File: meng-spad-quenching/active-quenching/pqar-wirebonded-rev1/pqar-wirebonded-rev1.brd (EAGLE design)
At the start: 46 x 46 mm, 62 parts, among them IC1 NL17SZ125, IC2 LTC1711, IC20 NC7WZ16P6X, IC3 NC7SV74K8X, IC4 BCV62, IC5 74AHC1G14DCK, IC6 SPAD, IC7 74AUC1G32DCK, IC8 74LVC1G02DCK, U1 SN74LVC1G123DCUT, X1 V_A, X2 OUT, X3 V_LOGIC, X4 I_HOLDOFF, X5 FORCE_QUENCH

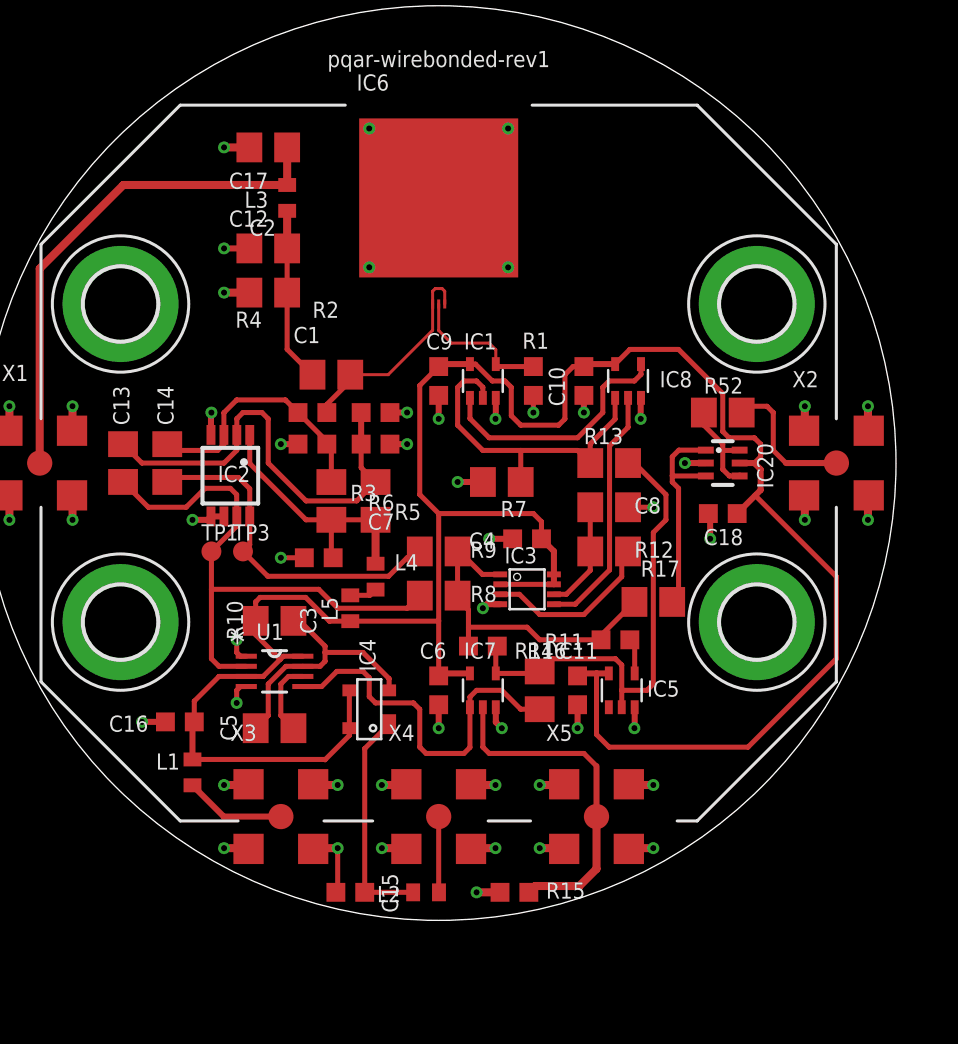
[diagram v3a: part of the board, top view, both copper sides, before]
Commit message: Clean up routing, DRC pass
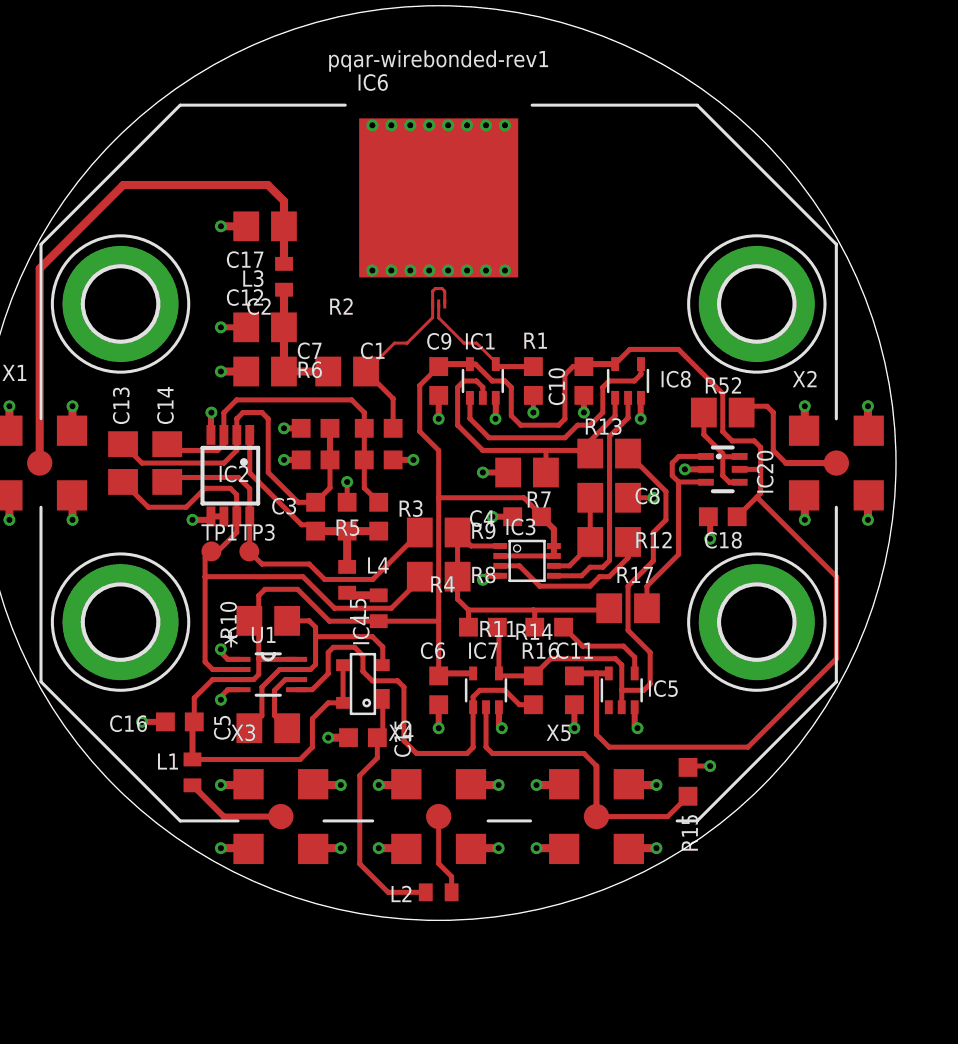
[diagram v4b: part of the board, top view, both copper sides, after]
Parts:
- R16: device rcl-modified-footprints:R0805 -> rcl-modified-footprints:R0603
- R3, R5: value RES SMD 1K OHM 1% 1/10W 0805 -> RES SMD 1K OHM 1% 1/10W 0603; device rcl-modified-footprints:R0805 -> rcl-modified-footprints:R0603
- moved R15 10.3 mm to (12.5, -16.0), turned to 90 degrees
- moved C15 7.80 mm to (-3.81, -13.8)
- moved C12 3.97 mm to (-8.73, 6.83)
- moved C17 3.97 mm to (-8.73, 11.9)
- moved C2 3.97 mm to (-8.73, 4.60)
- moved L3 3.97 mm to (-7.78, 9.37)
- moved R6 3.84 mm to (-6.19, 0.16), turned to 180 degrees
- moved C1 3.43 mm to (-3.02, 1.75)
- moved R4 3.43 mm to (-3.02, 0.16), turned to 0 degrees
- moved R11 3.39 mm to (5.56, -8.26)
- moved C7 3.12 mm to (-6.19, 1.75), turned to 180 degrees
- moved R5 3.12 mm to (-6.19, -2.70)
- moved C3 2.51 mm to (-4.60, -2.70), turned to 90 degrees
- moved R3 2.51 mm to (-3.02, -2.70)
- moved L4 1.44 mm to (-4.60, -5.87)
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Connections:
- net N$1 renamed VDD_COMP_JUMP
- net N$2 renamed CLK_RESET_JUMP
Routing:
- net KATHODE_C: track 13.3 -> 17.1 mm
- net !QUENCH: track 1.79 -> 5.02 mm
- net AV_DET_REF: track 22.4 -> 19.5 mm
- net V_A_FILT: track 9.19 -> 6.34 mm
- net QUENCH: track 24.5 -> 26.5 mm
- net HOLDOFF_TIMER: track 18.8 -> 20.8 mm
- net CLK_RESET: track 17.1 -> 15.4 mm
- net FORCE_QUENCH: track 17.2 -> 15.5 mm
- net AV_DET: track 28.6 -> 30.1 mm
- net V_A: track 25.9 -> 27.3 mm
- net I_HOLDOFF_FILT: track 11.4 -> 12.7 mm
- net RESET: track 12.6 -> 11.7 mm
- net VDD_COMP: track 13.1 -> 12.3 mm
- net ANODE: track 7.27 -> 6.53 mm
- net !RESET_RC: track 5.50 -> 4.80 mm
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
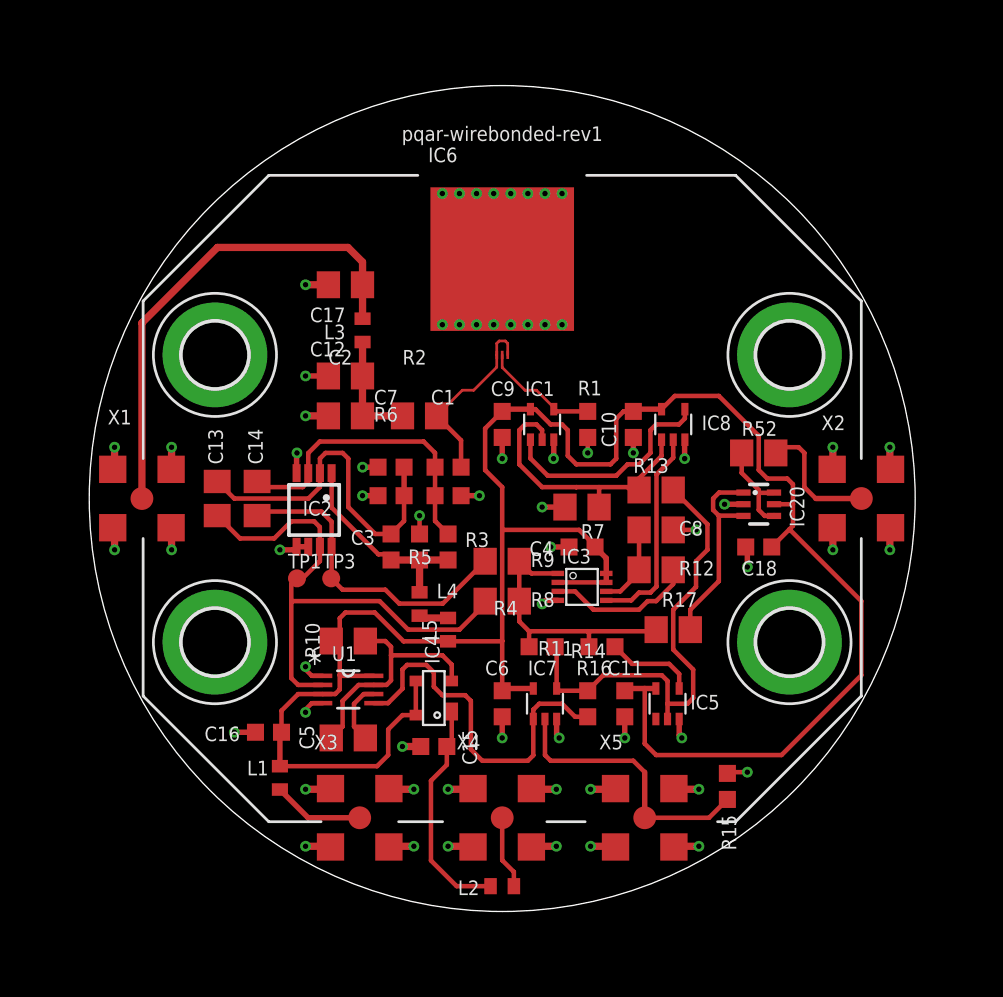
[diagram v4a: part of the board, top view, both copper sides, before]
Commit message: started silkscreen cleanup
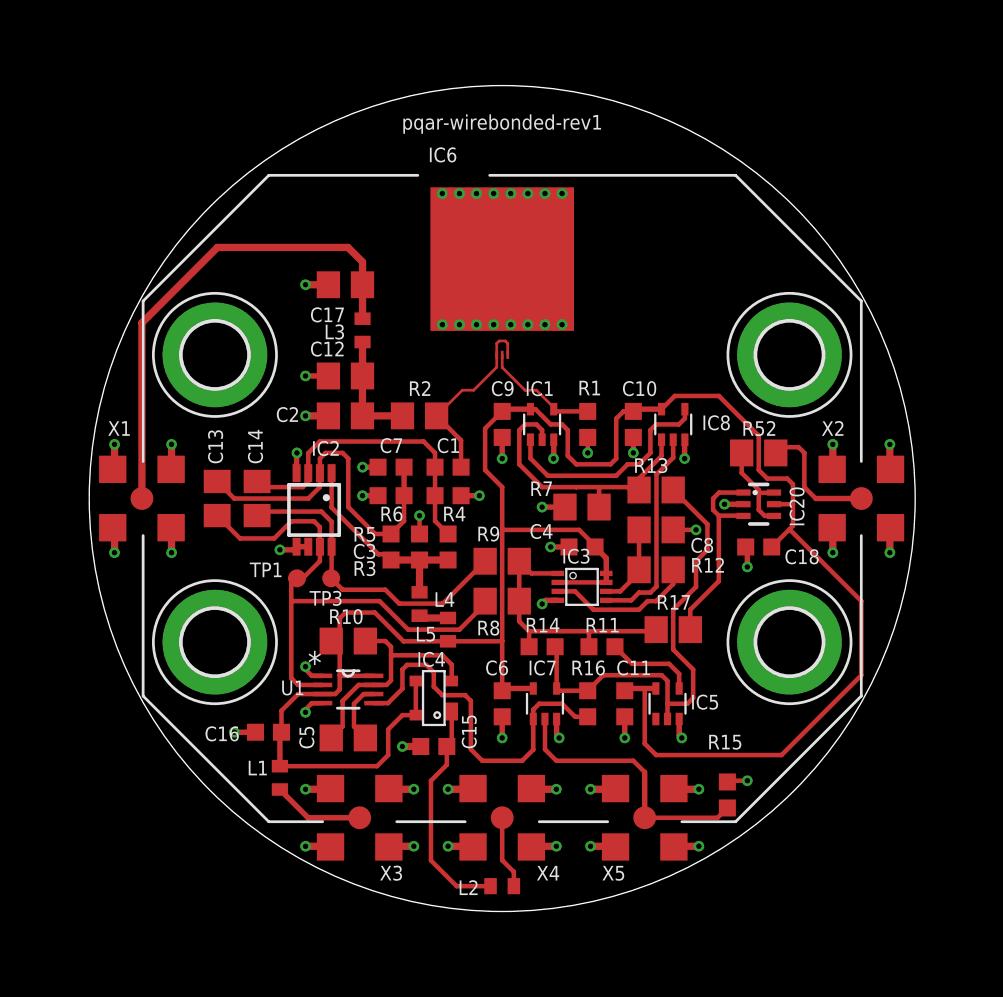
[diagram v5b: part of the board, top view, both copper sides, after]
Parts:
- moved R15 0.48 mm to (12.5, -16.5)
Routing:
- net GND: track 64.5 -> 65.8 mm

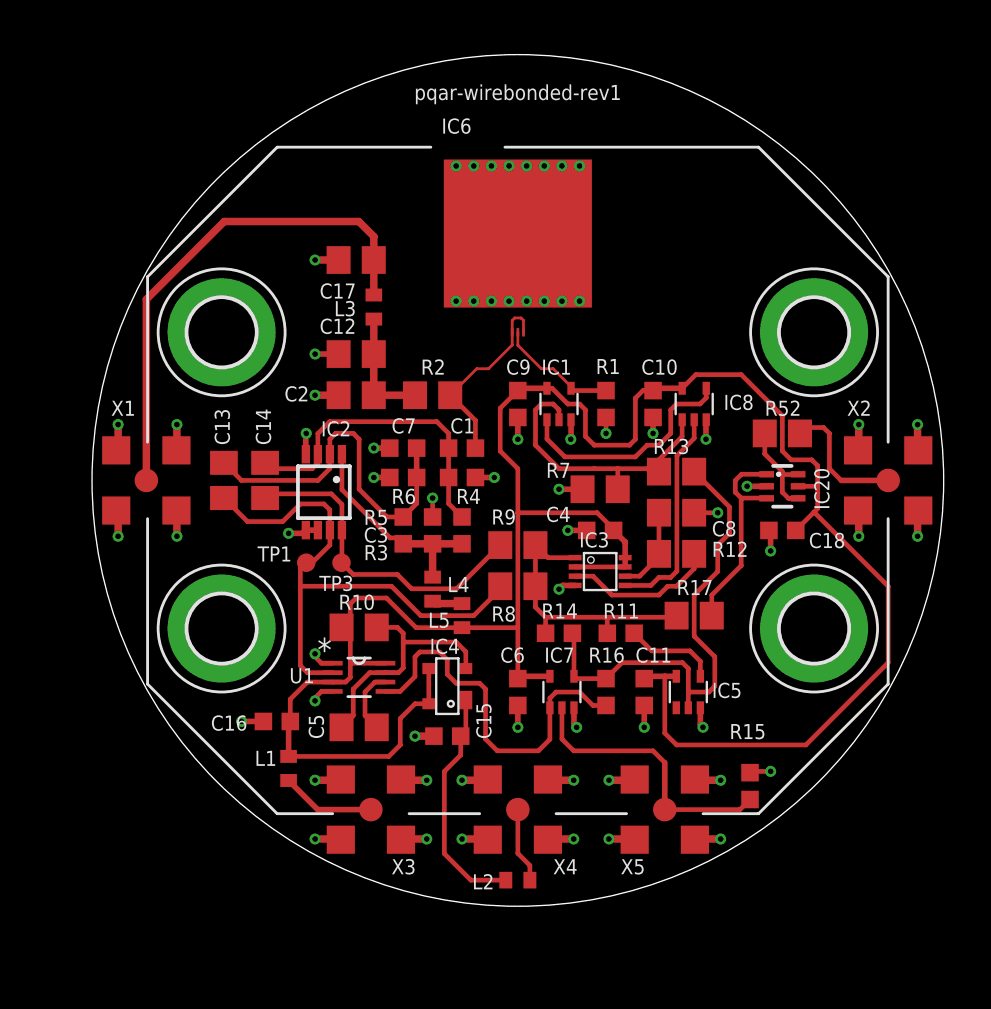
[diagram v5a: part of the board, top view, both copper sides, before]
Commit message: Cleaned stop mask errors on silkscreen
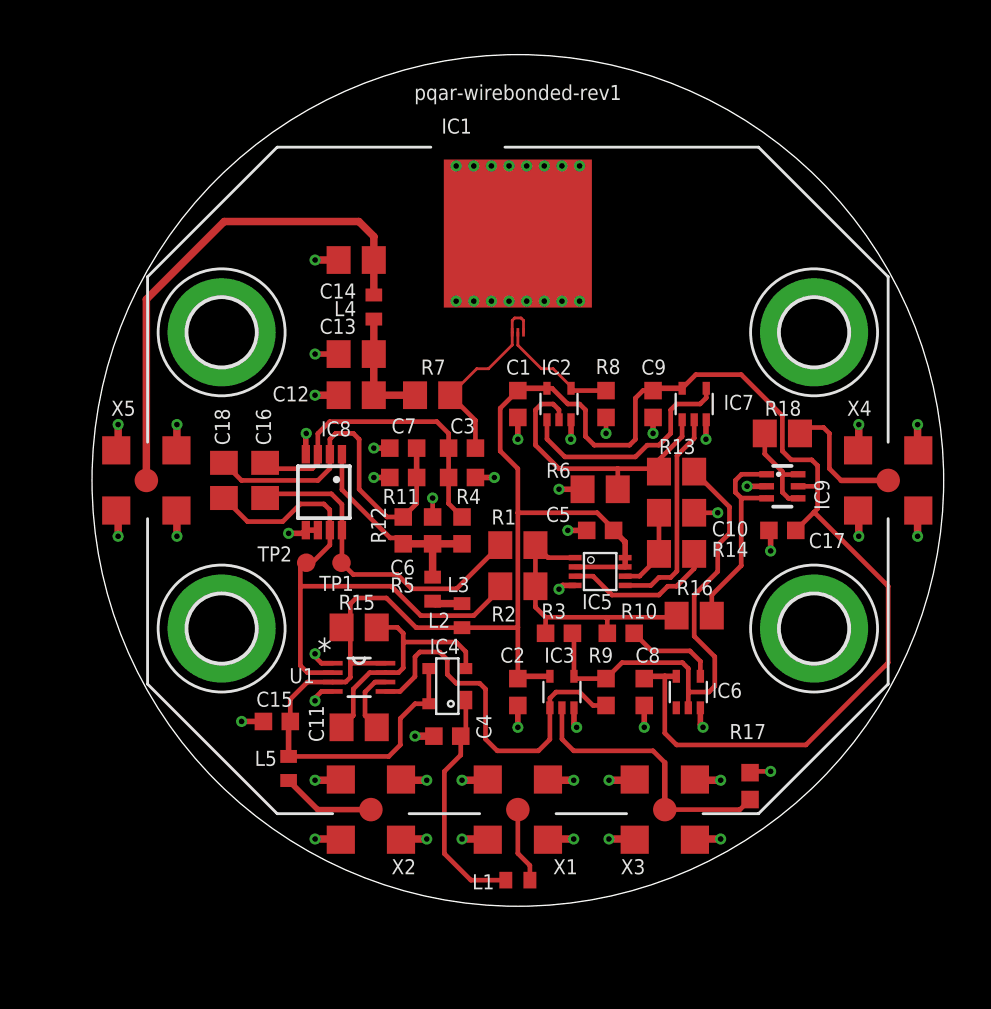
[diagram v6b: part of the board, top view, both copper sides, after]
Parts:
- removed TP3: AV_DET, testpad:TP10R
- added TP2: AV_DET, testpad:TP10R
- C1: value CAP CER 100PF 50V C0G 0603 5% -> IPDiA 935131425610
- C10, C16: value IPDiA 935131425610 -> DNP; device rcl-modified-footprints:C0603 -> rcl-modified-footprints:C0805
- C11: value IPDiA 935131425610 -> CAP CER 0.1UF 50V X7R 0805 5%; device rcl-modified-footprints:C0603 -> rcl-modified-footprints:C0805
- C13, C14: value DNP -> CAP CER 0.1UF 50V X7R 0805 5%
- C15: value CAP CER 0.1UF 50V X7R 0603 5% -> IPDiA 935131425610
- C17, C2, C5: value CAP CER 0.1UF 50V X7R 0805 5% -> CAP CER 0.1UF 50V X7R 0603 5%; device rcl-modified-footprints:C0805 -> rcl-modified-footprints:C0603
- C18: value CAP CER 0.1UF 50V X7R 0603 5% -> DNP; device rcl-modified-footprints:C0603 -> rcl-modified-footprints:C0805
- C3: value CAP CER 0.1UF 50V X7R 0603 5% -> CAP CER 100PF 50V C0G 0603 5%
- C8: value DNP -> IPDiA 935131425610; device rcl-modified-footprints:C0805 -> rcl-modified-footprints:C0603
- IC1: value NL17SZ125 -> SPAD; device 74xx-little-de:SC70-5 -> meng:SPAD-WIREBOND-GENERIC-CRYO
- IC2: value LTC1711 -> NL17SZ125; device meng:MSOP8 -> 74xx-little-de:SC70-5
- IC3: value NC7SV74K8X -> 74AUC1G32DCK; device meng:US8_3.1MM_JDEC_MO-187 -> 74xx-little-us:SC70-5
- IC5: value 74AHC1G14DCK -> NC7SV74K8X; device 74xx-little-us:SC70-5 -> meng:US8_3.1MM_JDEC_MO-187
- IC6: value SPAD -> 74AHC1G14DCK; device meng:SPAD-WIREBOND-GENERIC-CRYO -> 74xx-little-us:SC70-5
- IC7: value 74AUC1G32DCK -> 74LVC1G02DCK
- IC8: value 74LVC1G02DCK -> LTC1711; device 74xx-little-us:SC70-5 -> meng:MSOP8
- R1: value RES SMD 10M OHM 1% 1/10W 0603 -> DNP; device rcl-modified-footprints:R0603 -> rcl-modified-footprints:R0805
- R10: value DNP -> RES SMD 0R 0603; device rcl-modified-footprints:R0805 -> rcl-modified-footprints:R0603
- R11: value RES SMD 0R 0603 -> RES SMD 1K OHM 1% 1/10W 0603
- R12: value RES SMD 0R 0805 -> RES SMD 1K OHM 1% 1/10W 0603; device rcl-modified-footprints:R0805 -> rcl-modified-footprints:R0603
- R14, R16: value DNP -> RES SMD 0R 0805; device rcl-modified-footprints:R0603 -> rcl-modified-footprints:R0805
- R15: value RES SMD 10K OHM 1% 1/10W 0603 -> DNP; device rcl-modified-footprints:R0603 -> rcl-modified-footprints:R0805
- R17: value RES SMD 0R 0805 -> RES SMD 10K OHM 1% 1/10W 0603; device rcl-modified-footprints:R0805 -> rcl-modified-footprints:R0603
- R2: value RES SMD 1K OHM 1% 1/10W 0805 -> DNP
- R3: value RES SMD 1K OHM 1% 1/10W 0603 -> DNP
- R6: value RES SMD 1K OHM 1% 1/10W 0603 -> DNP; device rcl-modified-footprints:R0603 -> rcl-modified-footprints:R0805
- R7: value DNP -> RES SMD 1K OHM 1% 1/10W 0805
- R8: value DNP -> RES SMD 10M OHM 1% 1/10W 0603; device rcl-modified-footprints:R0805 -> rcl-modified-footprints:R0603
- R9: device rcl-modified-footprints:R0805 -> rcl-modified-footprints:R0603
- X1: value V_A -> I_HOLDOFF
- X2: value OUT -> V_LOGIC
- X3: value V_LOGIC -> FORCE_QUENCH
- X4: value I_HOLDOFF -> OUT
- X5: value FORCE_QUENCH -> V_A
- moved X5 33.2 mm to (-20.1, 0.00)
- moved X2 33.1 mm to (-7.94, -17.8)
- moved C18 30.3 mm to (-15.9, 0.00), turned to 270 degrees
- moved C17 27.3 mm to (14.3, -2.70)
- moved X1 26.8 mm to (0.00, -17.8)
- moved X4 26.8 mm to (20.0, 0.00)
- moved IC6 26.4 mm to (9.21, -11.4)
- moved R15 22.8 mm to (-8.57, -7.94), turned to 0 degrees
- moved IC8 20.6 mm to (-10.5, -0.64), turned to 180 degrees
- moved C2 18.3 mm to (0.00, -11.4), turned to 270 degrees
- moved IC7 17.1 mm to (9.53, 4.13)
- moved C5 16.8 mm to (4.45, -2.70), turned to 180 degrees
- moved X3 15.9 mm to (7.94, -17.8)
- moved L3 15.6 mm to (-4.60, -5.87), turned to 90 degrees
- moved L4 15.6 mm to (-7.78, 9.37), turned to 270 degrees
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- renumbered IC20 to IC9, R52 to R18
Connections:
- net !AV_DET: now also C16.2, IC8.8, R1.1, TP1.TP; no longer C14.2, IC2.8, R9.1, TP3.TP
- net !EN_DRIVER: now also IC2.1, IC7.4; no longer IC1.1, IC8.4
- net !QUENCH: now also IC6.4, R10.2; no longer IC5.4, R11.2
- net !RESET: now also IC5.3, R14.1; no longer IC3.3, R12.1
- net !RESET_RC: now also C10.1, IC5.6, R14.2; no longer C8.1, IC3.6, R12.2
- net +5V: now also C1.1, C15.1, C17.1, C2.1, C5.1, C8.1, IC2.5, IC3.5, IC5.2, IC5.7, IC5.8, IC6.5, L2.1, L5.2, R15.1; no longer C10.1, C11.1, C16.1, C18.1, C4.1, C6.1, IC1.5, IC3.2, IC3.7, IC3.8, IC5.5, IC8.5, L1.2, L5.1, R10.1
- net ANODE: now also IC1.A, IC2.4, R8.1; no longer IC1.4, IC6.A, R1.1
- net AV_DET: now also C18.2, IC8.7, R2.1, TP2.TP; no longer C13.2, IC2.7, R8.1, TP1.TP
- net AV_DET_REF: now also C18.1, IC8.2, R11.1, R12.2; no longer C13.1, IC2.2, R5.2, R6.1
- net CEXT: now also C11.2; no longer C5.2
- net CLK_RESET: now also IC5.1, R1.2, R10.1, R16.1, R2.2, R3.1; no longer IC3.1, R11.1, R14.1, R17.1, R8.2, R9.2
- net CLK_RESET_JUMP: now also R16.2; no longer R17.2
- net DRIVER_IN: now also IC2.2, IC7.1, R6.1; no longer IC1.2, IC8.1, R7.1
- net FORCE_QUENCH: now also IC3.2, R17.1, X3.S; no longer IC7.2, R15.1, X5.S
- net GND: now also C1.2, C13.2, C14.2, C5.2, IC1.GND, IC2.3, IC3.3, IC5.4, IC6.3, IC8.4, IC8.5, IC8.6, R11.2, R17.2, R8.2; no longer C11.2, C16.2, C18.2, C3.2, IC1.3, IC2.4, IC2.5, IC2.6, IC3.4, IC5.3, IC6.GND, IC8.3, R1.2, R15.2, R7.2
- net HOLDOFF_CAP: now also C11.1, R15.2; no longer C5.1, R10.2
- net HOLDOFF_TIMER: now also IC3.1, R9.2; no longer IC7.1, R16.2
- net I_HOLDOFF: now also L1.1, X1.S; no longer L2.1, X4.S
- net I_HOLDOFF_FILT: now also C4.1, L1.2; no longer C15.1, L2.2
- net KATHODE: now also C3.1, IC1.K1, IC1.K2, R7.2; no longer C1.1, IC6.K1, IC6.K2, R2.2
- net KATHODE_C: now also C16.1, C3.2, IC8.3, R5.2; no longer C1.2, C14.1, IC2.3, R3.2
- net OUT_R: now also X4.S; no longer X2.S
- net QUENCH: now also IC3.4, IC6.2, R3.2, R9.1; no longer IC5.2, IC7.4, R14.2, R16.1
- net RESET: now also IC5.5, IC7.2; no longer IC3.5, IC8.2
- net VDD_COMP: now also C6.1, IC8.1, L3.2, R12.1; no longer C3.1, IC2.1, L4.2, R3.1
- net VDD_COMP_JUMP: now also L2.2, L3.1; no longer L4.1, L5.2
- net V_A: now also C14.1, L4.1, X5.S; no longer C17.1, L3.1, X1.S
- net V_A_FILT: now also C13.1, L4.2, R7.1; no longer C2.1, L3.2, R2.1
- net V_LOGIC: now also L5.1, X2.S; no longer L1.1, X3.S
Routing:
- net DRIVER_IN: track 17.1 -> 15.7 mm
